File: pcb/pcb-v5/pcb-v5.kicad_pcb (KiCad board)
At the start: 2 copper layers, 14 parts, among them J1 Conn_01x05_Female, J2 Conn_01x05_Female, J3 Conn_01x05_Female, J4 Conn_01x05_Male, SW1 G71Y, SW2 G71Y, SW3 G71Y, U1 AMS1117-3.3

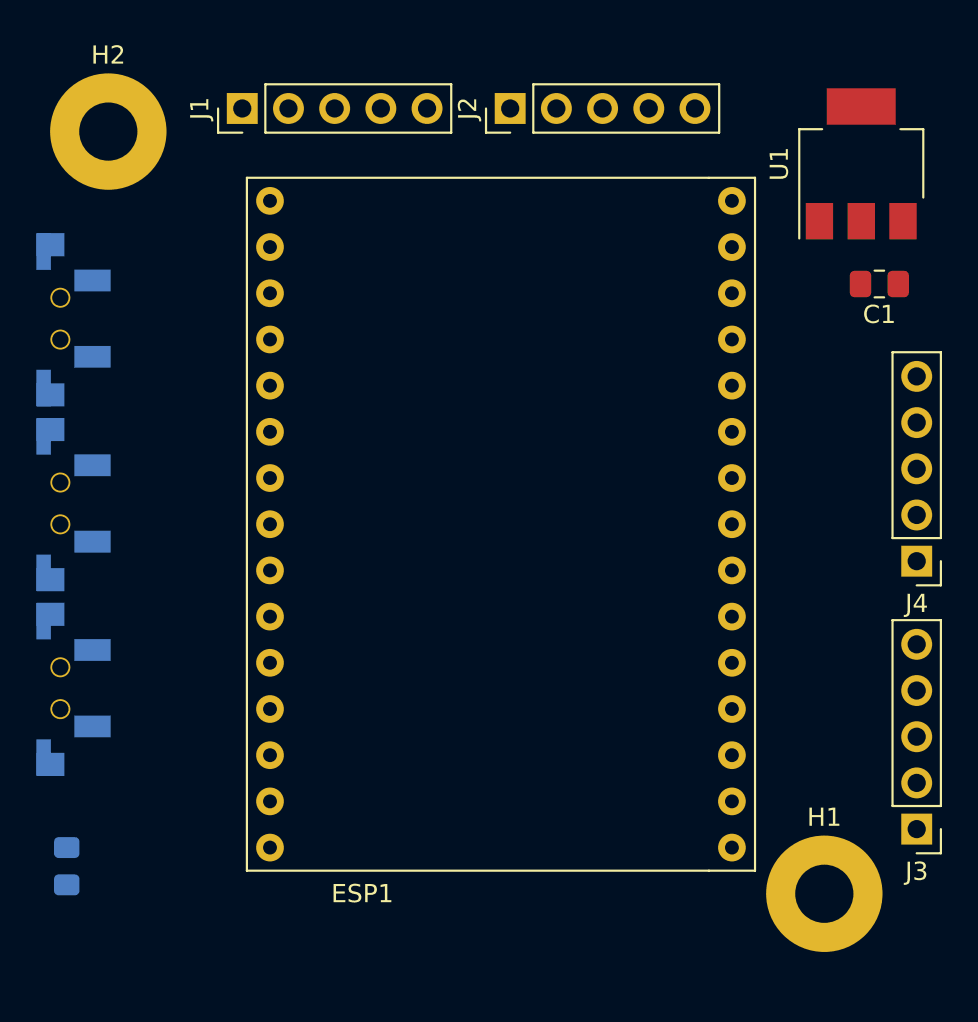
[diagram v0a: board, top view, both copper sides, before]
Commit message: PCB-V5 update
Changed buttons and pins location.
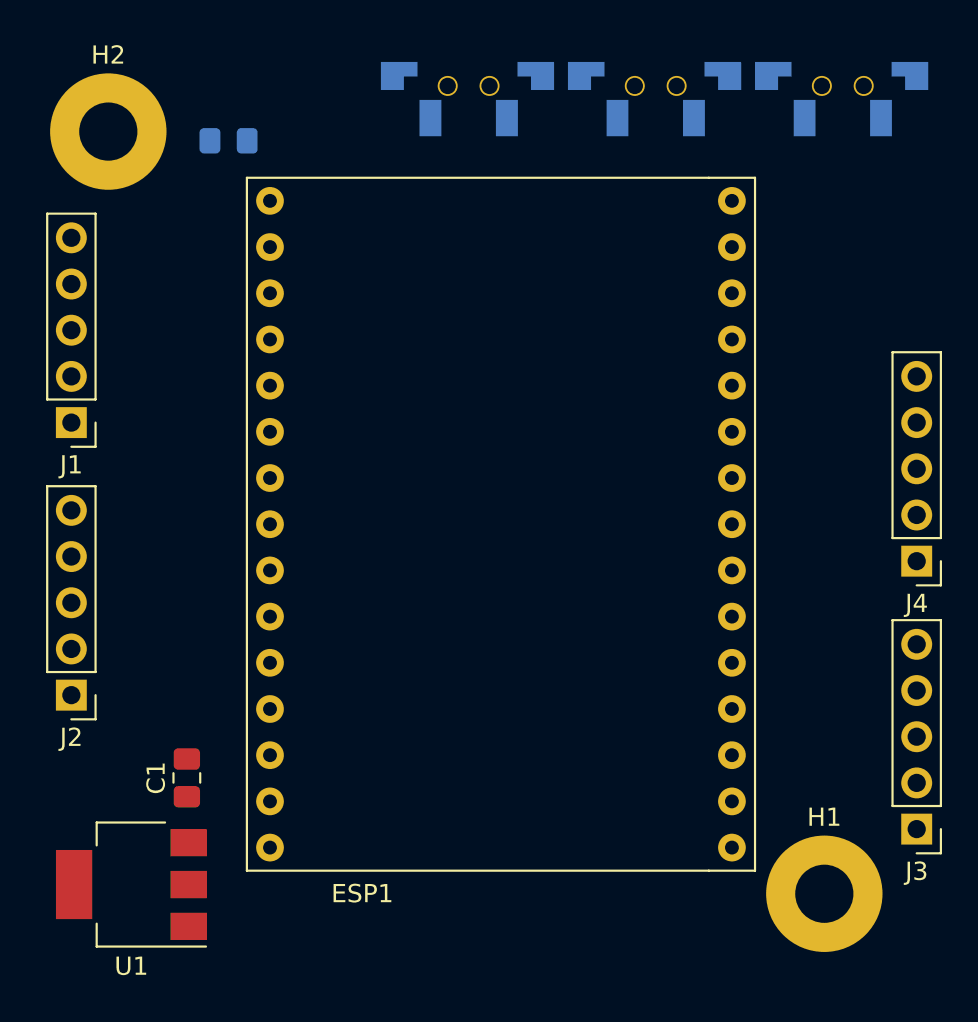
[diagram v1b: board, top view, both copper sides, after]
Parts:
- moved U1 56.4 mm to (132.1, 106.2), turned to 180 degrees
- moved SW1 56.1 mm to (171.1, 61.0), turned to 180 degrees
- moved C1 46.8 mm to (135.1, 100.3), turned to 90 degrees
- moved SW2 41.8 mm to (160.8, 61.0), turned to 180 degrees
- moved D1 40.9 mm to (137.4, 65.3), turned to 0 degrees
- moved J2 40.3 mm to (128.8, 95.8), turned to 180 degrees
- moved SW3 27.6 mm to (150.5, 61.0), turned to 180 degrees
- moved J1 19.7 mm to (128.8, 80.8), turned to 180 degrees
